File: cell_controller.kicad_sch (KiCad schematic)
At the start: 1 part, among them U1 BQ78350DBT

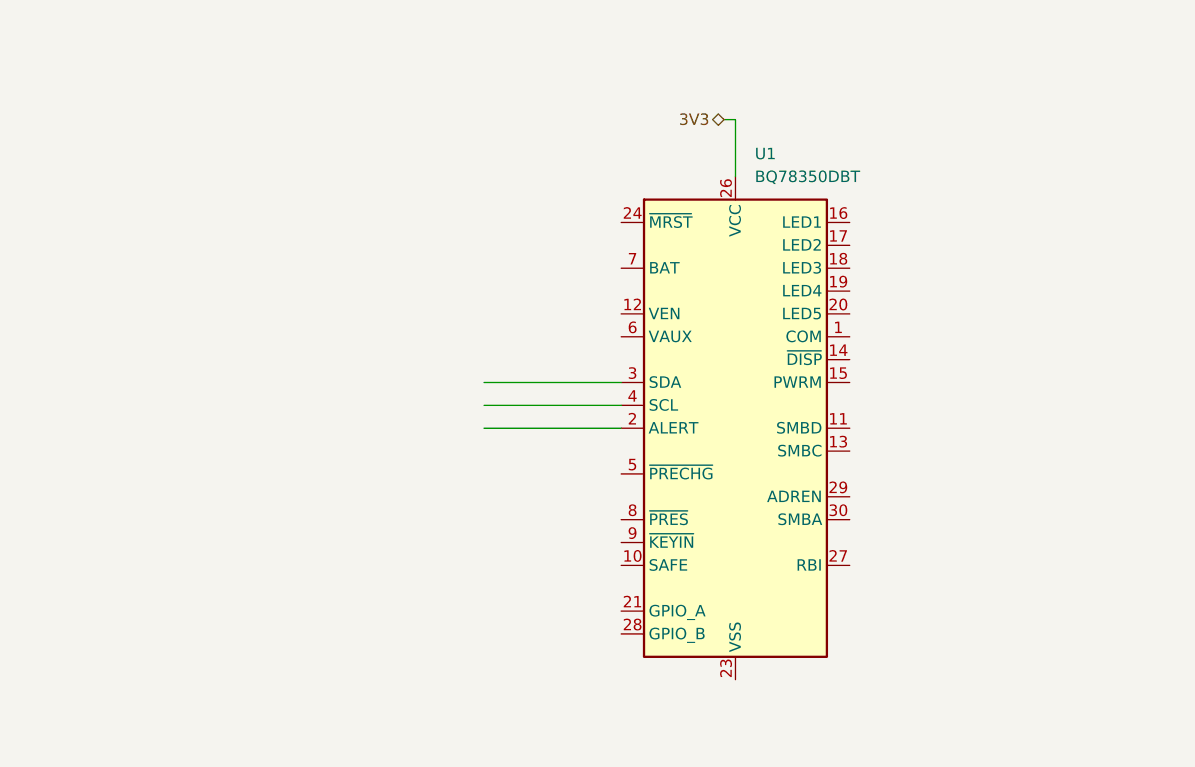
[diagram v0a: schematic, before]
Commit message: beginning fuel gage layout
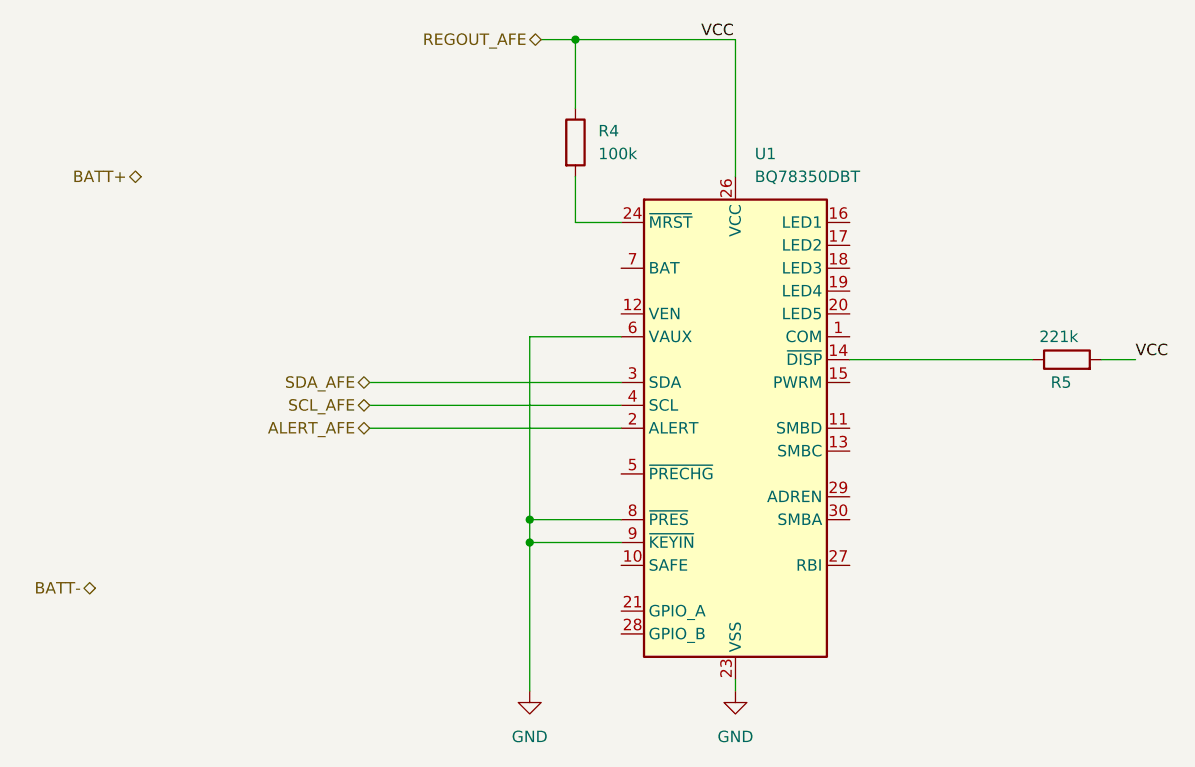
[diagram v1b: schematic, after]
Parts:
- added R4: 100k, symbol Device:R
- added R5: 221k, symbol Device:R
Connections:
- net at U1.14 (~{DISP}): now also R5.1
- net ALERT_AFE: now reaches U1.2 (ALERT)
- net GND: now reaches U1.22 (VSS), U1.23 (VSS), U1.25 (VSS)
- net GND: now also U1.6 (VAUX), U1.8 (~{PRES}), U1.9 (~{KEYIN})
- net at U1.24 (~{MRST}): now also R4.2
- net SDA_AFE: now reaches U1.3 (SDA)
- net SCL_AFE: now reaches U1.4 (SCL)
- net 3V3 renamed REGOUT_AFE
- net REGOUT_AFE: now also R4.1, R5.2

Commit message: .
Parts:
- added Q1, Q2: BSS84, Package_TO_SOT_SMD:SOT-23, symbol Transistor_FET:BSS84
- added R6, R8: 100k, symbol Device:R
- added R7: 300k, symbol Device:R
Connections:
- net BATT+: now also Q1.2 (S), R6.1
- new net: Q1.1 (G), R6.2, R8.1
- new net: Q1.3 (D), R7.1

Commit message: progress
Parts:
- added D2, D3, D4, D5, D6: LED, symbol Device:LED
- added R41, R42, R43, R44: R, symbol Device:R
- R5: value 221k -> R
- renumbered Q2 to Q1, Q1 to Q2, R7 to R1, R6 to R2, R8 to R3
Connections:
- net GND: now also U1.14 (~{DISP})
- net REGOUT_AFE: now also R41.2, R42.2, R43.2, R44.2
- net at R5.1: now also D2.2 (A); no longer U1.14 (~{DISP})
- net at U1.16 (LED1): now also D2.1 (K)
- net at U1.17 (LED2): now also D3.1 (K)
- net at U1.18 (LED3): now also D4.1 (K)
- net at U1.19 (LED4): now also D5.1 (K)
- net at U1.20 (LED5): now also D6.1 (K)
- new net: D6.2 (A), R44.1
- new net: D5.2 (A), R43.1
- new net: D4.2 (A), R42.1
- new net: D3.2 (A), R41.1
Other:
- moved on the sheet: R4, U1

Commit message: progress on cell fuel gage
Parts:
- removed R41, R42, R43, R44: R, symbol Device:R
- added C4: 3300pF, symbol Device:C
- added C5: 0.1u, symbol Device:C
- added R10, R11, R12, R13: 10, symbol Device:R
- added R9: 13.7k, symbol Device:R
- D2: value LED -> 599-2100-137F; footprint (none) -> LED_SMD:LED_1210_3225Metric
- R5: value R -> 10
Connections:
- net GND: now also Q1.3 (D), C4.2, C5.2, R9.2
- net REGOUT_AFE: now also R5.1, C5.1, R10.1, R11.1, R12.1, R13.1; no longer R5.2
- net BAT: now reaches R1.2
- net BAT: now also U1.7 (BAT), C4.1, R9.1
- net at D6.2 (A): now also R13.2
- net LED5: now reaches D6.1 (K), U1.20 (LED5)
- net at D2.2 (A): now also R5.2; no longer R5.1
- net at D5.2 (A): now also R12.2
- net at D4.2 (A): now also R11.2
- net at R3.2: now also Q1.2 (S)
- net LED2: now reaches D3.1 (K), U1.17 (LED2)
- net at D3.2 (A): now also R10.2
- net VEN: now reaches U1.12 (VEN)
- net VEN: now also Q1.1 (G)
- net LED1: now reaches D2.1 (K), U1.16 (LED1)
- net LED3: now reaches D4.1 (K), U1.18 (LED3)
- net LED4: now reaches D5.1 (K), U1.19 (LED4)
- no-connect marks 0 -> 2
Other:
- note added: "25ppm/C"
- note added: "no precharge FET required - NC?"
- moved on the sheet: Q1, Q2, R1, R2, R3

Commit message: updates
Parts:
- added C6: 0.1u, symbol Device:C
- added D7, D8: 5.6V, symbol Device:D_Zener
- added D9: 599-2100-137F, LED_SMD:LED_1210_3225Metric, symbol Device:LED
- added J2: Conn_01x03_Pin, symbol Connector:Conn_01x03_Pin
- added R14, R15: 100, symbol Device:R
- added R17: 10, symbol Device:R
- added TP1: TestPoint_2Pole, Jumper:SolderJumper-2_P1.3mm_Open_RoundedPad1.0x1.5mm, symbol Connector:TestPoint_2Pole
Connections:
- net GND: now also U1.30 (SMBA), C6.2, D7.2 (A), D8.2 (A), J2.3 (Pin_3), TP1.1
- net REGOUT_AFE: now also R17.1
- net at R4.2, U1.24 (~{MRST}): now also TP1.2
- net SMBD: now reaches U1.11 (SMBD)
- net SMBD: now also D7.1 (K), R14.1
- net SMBC: now reaches U1.13 (SMBC)
- net SMBC: now also D8.1 (K), R15.1
- net PWRM: now reaches U1.15 (PWRM)
- net PWRM: now also D9.1 (K)
- net HS_SW_CP_EN: now reaches U1.21 (GPIO_A)
- net at U1.27 (RBI): now also C6.1
- net HS_SW_PMON_EN: now reaches U1.28 (GPIO_B)
- net HS_SW_PCHG_EN: now reaches U1.5 (~{PRECHG})
- new net: J2.2 (Pin_2), R15.2
- new net: D9.2 (A), R17.2
- new net: J2.1 (Pin_1), R14.2
- no-connect marks 2 -> 3
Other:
- note added: "No SMBUS configuration required"
- note added: "No external display"
- note added: "No other fuel gages in system"
- note added: "is this correct?"
- note added: "no insertion detection required"
- note added: "no need this for user control over battery connection (e.g. ebike)"
- note added: "no secondary protection mechanism to control"
- note removed: "no precharge FET required - NC?"
- moved on the sheet: C5, D2, D3, D4, D5, D6, R10, R11, R12, R13, R4, R5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

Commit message: structural changes
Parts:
- removed Q1, Q2: BSS84, Package_TO_SOT_SMD:SOT-23, symbol Transistor_FET:BSS84
- added Q1: NMOS, symbol Simulation_SPICE:NMOS
- added Q2: PMOS, symbol Simulation_SPICE:PMOS
- added R22: 1M, symbol Device:R
- R9: value 13.7k -> 16k
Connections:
- net BATT+: now also Q2.1 (D)
- net GND: now also Q1.3 (S)
- net REGOUT_AFE: now also R22.1
- net VEN: now also Q1.2 (G), R22.2
- net at R2.2, R3.1: now also Q2.2 (G)
- net at R1.1: now also Q2.3 (S)
- net at R3.2: now also Q1.1 (D)
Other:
- note added: "Required to program the chip"
- note added: "rated to 50V"

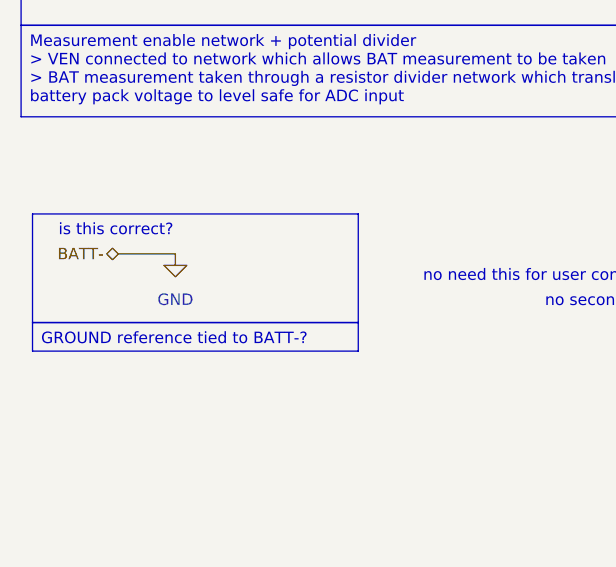
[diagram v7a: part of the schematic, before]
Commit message: refinements - moving battery pack off the PCB
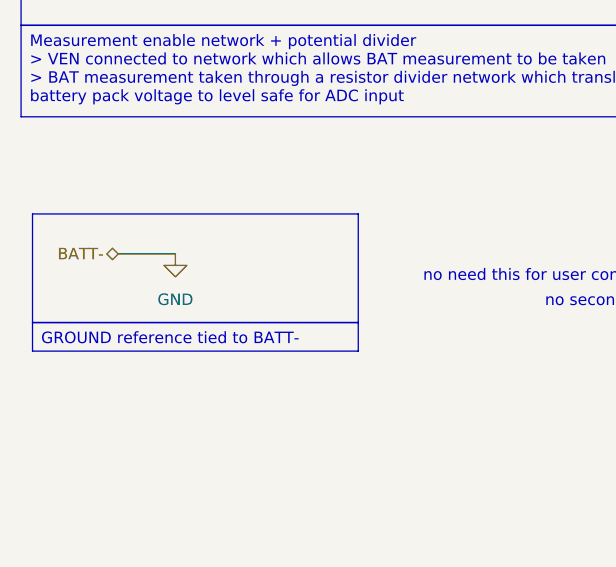
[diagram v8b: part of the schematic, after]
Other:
- note removed: "is this correct?"
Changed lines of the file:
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@@
 		)
 	)
-	(text "is this correct?"
-		(exclude_from_sim no)
-		(at 25.146 101.6 0)
-		(effects
-			(font
-				(size 1.27 1.27)
-				(color 255 26 68 1)
-			)
-		)
-	)
 	(text "No other fuel gages in system"
 		(exclude_from_sim no)
@@
 		)
 	)
-	(text_box "GROUND reference tied to BATT-?"
+	(text_box "GROUND reference tied to BATT-"
 		(exclude_from_sim no)
 		(at 15.875 111.76 0)
@@
 			"dQBEAE8AUQArAE0AMgBEAG4AMwBHAGEAZgBIADYAdgBlAEMAQwBBAGQATgBSAFoAdgBqAFIAcQBx"
 			"AG8AQgB1AEIAeAB1AC8ANwA5ACsAKwBMAEcANgBmAFAATQBrADUAVQA5AHoANwBhAFgAMQAyAGMA"
-			"MgB2AHcAdwBaAGgAZAB2AFYAbwBqAEEAegAyAHcASAA3AEoAUwBWAA=="
+			"MgB2AHcAdwBaAGgAZAB2AFYAbwBqAEEAegAyAHcASAA3AEoAUwBWAHgAZwBrAEEAawBVAGcARQA4"
+			"ADMANQAwAEIAOABhAE8ARwA0AFAAVwBlAEMAZAAyAC8AbgA0AEgATgBsAGQAWABXADAATAAwAEYA"
+			"OQBWAFAAbwBpAEMAVQBqAGEAYQBtADQAMwBqADgAMABTAGYATgBwAGcASgA0AHUAUABWAHQAOAAr"
+			"AFkAaQBHAG8AMgBaAE4ASgBpADgAbgB5AHUAUQBOAGIAMwBtAFIANwBWAC8AdgBYAHkAeQBaAFYA"
+			"RQB3AEkAbwBvAFQAUwBEAGUAQwA5AG8ANABPADAAOABlADEAcQB6AGQANABLAFUAYQBEAFEAYgBP"
+			"AHoARAB4ADgANQBDAGwAVwBUAHEAagBCAHYAdwBXAHkARQB3AHcAWAA0AHcAKwA5ACsAbAA2AEUA"
+			"WgA2ADMAMwBZAGYAMABJAFMAawBVAGoARQBjAG4AaQBxAFYAcQB3AFIAaABCAHcAUAB2ADQAeABp"
+			"AGcATAAwADQAOAAvAEoAeQB6AFcAYgAwAGwAMwBjAFAANABhAG8AZgBYAEkAUABwAE0ANgBiADUA"
+			"agBrAFgAMQBFADUAdQB4ADkAZgBuAGYAbQBQADkAMQBnADkASABvAEwAdABXAGcAeQBGADcAUQBz"
+			"AEgAVgBxAFgAcQA0ADEANABBAFoAcgA2AEcATABrAGUAVwBwAHEAOAB4AHoAUwB2AGMAegB6AEIA"
+			"ZABJADgAWQBFAFkARgBxAGkATwBLAHYAegBYAFUAMgB0AFcAKwB6AGQAZwBJAHIAQgBFAE0AMgBL"
+			"AHcAUgBIAG0AcwBsAE0AbgBKAE0AZQBKAGQAQgA0AFQASQB5ADIARgBjAE4ASABIAEUAYgB4ADQA"
+			"SABqAHIAUgBhAEcAbQAyADEAUgBqADcAYwBxAHAAZQBmAG0AVwBtAGsANQBhAGYAcAB6AGYAbwBa"
+			"AEMANgBYAEIAdABWAGkAYwBQAEIAQQBLAEcAQgBRAFkAQQBaAHcAOAA1AEIAKwA4AGQALwBwAHQA"
+			"UgBUAEIATABKAHAAUABsACsAMQBOAGYAUABSADAAdABMAEMANABZAE4AcgA4AFQAMgBGADcAWgA1"
+			"AHAASQBLAFcAbQBKAFUANABhAGUAVABYAEwAegBUAEoAbQBRAFkATQBMAEEAUABnAEsAUQBFAGoA"
+			"UgBuAG0AaAAzAFQAdAAzAHYARwBxAEMANwAwAGEATQBIAEcAYQBpAFYAMwBmAHUAZQBCAFcAQQBi"
+			"AFkAMQB6AEgAaABpAHMAWABHAEEATQBDAHUAWgBRAEsARwBUADQAMABaAC8AVwBTAGYAaQBaAFEA"
+			"eAB6AE0AQgAzADMANAByADMAOABHAGsAQQA0AHQAegBjADMASgB3AA=="
 		)
 	)
